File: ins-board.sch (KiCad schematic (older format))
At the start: 83 parts, among them P1 POWER, Q1 FDN306P, Q2 FDC638APZ, Q3 MOSFET_P, U1 24LC128, U2 STM32F415RGT6, U3 LTC4412, U4 MAX3051, U5 LT1965, U6 LT1761-3.3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

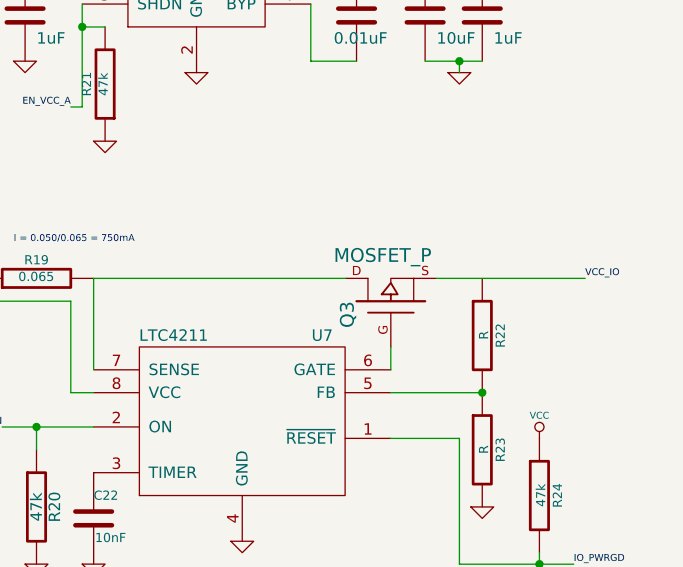
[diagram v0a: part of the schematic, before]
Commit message: add mosfet for current limiter
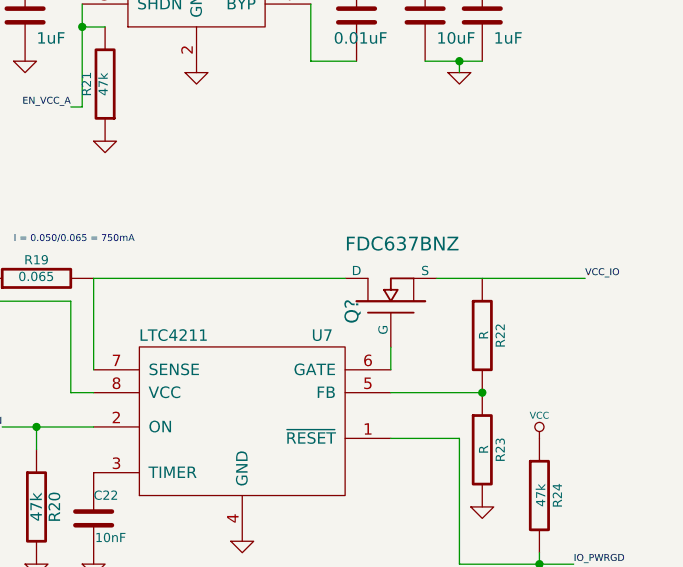
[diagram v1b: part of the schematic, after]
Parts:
- removed Q3: MOSFET_P, ~, symbol MOSFET_P
- added Q?: FDC637BNZ, ~, symbol MOSFET_N
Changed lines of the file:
@@
-$EndComp
-$Comp
-L MOSFET_P Q3
-U 1 1 519731AD
-P 9700 5800
-F 0 "Q3" H 9700 5990 60  0000 R CNN
-F 1 "MOSFET_P" V 9900 6050 60  0000 R CNN
-F 2 "~" H 9700 5800 60  0000 C CNN
-F 3 "~" H 9700 5800 60  0000 C CNN
-	1    9700 5800
-	0    -1   -1   0
 $EndComp
 $Comp
@@
 Text Notes 4450 6300 0    20   ~ 0
 needed for ST USB-Bootloader
+$Comp
+L MOSFET_N Q?
+U 1 1 5197C0F0
+P 9700 5800
+F 0 "Q?" H 9710 5970 60  0000 R CNN
+F 1 "FDC637BNZ" V 9950 6000 60  0000 R CNN
+F 2 "~" H 9700 5800 60  0000 C CNN
+F 3 "~" H 9700 5800 60  0000 C CNN
+	1    9700 5800
+	0    -1   -1   0
+$EndComp
 $EndSCHEMATC

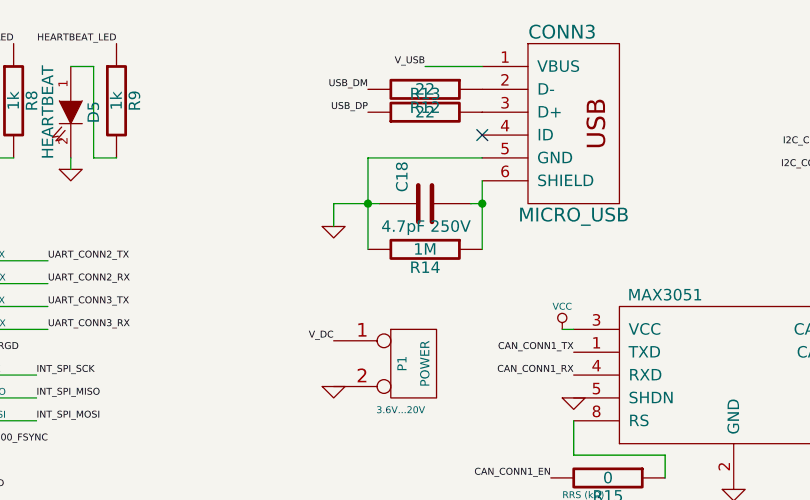
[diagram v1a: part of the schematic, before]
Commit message: remove usb shield connection
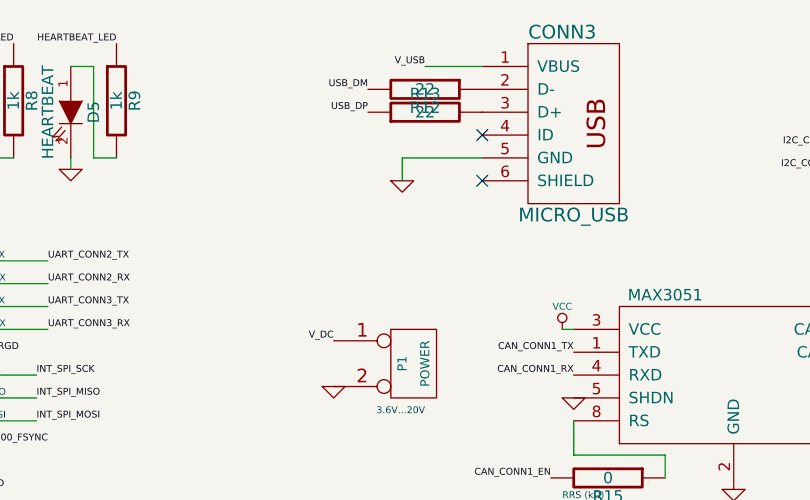
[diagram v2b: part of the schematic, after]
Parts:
- removed C18: 4.7pF 250V, symbol C
- removed R14: 1M, symbol R
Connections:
- wire segments 166 -> 162
- no-connect marks 2 -> 3
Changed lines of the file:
@@
 Sheet 1 2
 Title "INS BOARD"
-Date "18 may 2013"
+Date "17 may 2013"
 Rev "REV A"
 Comp ""
@@
 NoConn ~ 6200 1150
 $Comp
-L MICRO_USB CONN3
-U 1 1 517D9D13
-P 6550 1100
-F 0 "CONN3" H 6550 1500 60  0000 C CNN
-F 1 "MICRO_USB" H 6600 700 60  0000 C CNN
-F 2 "" H 6550 1100 60  0001 C CNN
-F 3 "ZX62-B-5PA(11)" H 6550 1100 60  0001 C CNN
-	1    6550 1100
-	1    0    0    -1
-$EndComp
-$Comp
 L VCC #PWR017
 U 1 1 517D7F9D
@@
 L GND #PWR021
 U 1 1 51295E18
-P 5550 1550
-F 0 "#PWR021" H 5550 1550 30  0001 C CNN
-F 1 "GND" H 5550 1480 30  0001 C CNN
-F 2 "" H 5550 1550 60  0001 C CNN
-F 3 "" H 5550 1550 60  0001 C CNN
-	1    5550 1550
-	1    0    0    -1
-$EndComp
-$Comp
-L C C18
-U 1 1 51295DDF
-P 5950 1450
-F 0 "C18" H 6000 1550 50  0000 L CNN
-F 1 "4.7pF 250V" V 5850 1250 50  0000 L CNN
-F 2 "" H 5950 1450 60  0001 C CNN
-F 3 "" H 5950 1450 60  0001 C CNN
-	1    5950 1450
-	0    -1   -1   0
-$EndComp
-$Comp
-L R R14
-U 1 1 51295DD1
-P 5950 1650
-F 0 "R14" V 6030 1650 50  0000 C CNN
-F 1 "1M" V 5950 1650 50  0000 C CNN
-F 2 "" H 5950 1650 60  0001 C CNN
-F 3 "" H 5950 1650 60  0001 C CNN
-	1    5950 1650
-	0    1    1    0
+P 5850 1350
+F 0 "#PWR021" H 5850 1350 30  0001 C CNN
+F 1 "GND" H 5850 1280 30  0001 C CNN
+F 2 "" H 5850 1350 60  0001 C CNN
+F 3 "" H 5850 1350 60  0001 C CNN
+	1    5850 1350
+	1    0    0    -1
 $EndComp
 $Comp
@@
 	5950 850  6200 850
 Wire Wire Line
-	5550 1550 5550 1450
-Wire Wire Line
-	5550 1450 5750 1450
-Wire Wire Line
-	6200 1250 5700 1250
-Wire Wire Line
-	5700 1250 5700 1650
-Wire Wire Line
-	6200 1350 6200 1650
-Wire Wire Line
 	2450 2400 800  2400
 Wire Wire Line
@@
 	800  2800 2450 2800
 Connection ~ 900  5850
-Wire Wire Line
-	6150 1450 6200 1450
-Connection ~ 6200 1450
-Connection ~ 5700 1450
 Wire Wire Line
 	4950 7300 4800 7300
@@
 	0    -1   -1   0
 $EndComp
+$Comp
+L MICRO_USB CONN3
+U 1 1 517D9D13
+P 6550 1100
+F 0 "CONN3" H 6550 1500 60  0000 C CNN
+F 1 "MICRO_USB" H 6600 700 60  0000 C CNN
+F 2 "" H 6550 1100 60  0001 C CNN
+F 3 "ZX62-B-5PA(11)" H 6550 1100 60  0001 C CNN
+	1    6550 1100
+	1    0    0    -1
+$EndComp
+Wire Wire Line
+	5850 1350 5850 1250
+Wire Wire Line
+	5850 1250 6200 1250
+NoConn ~ 6200 1350
 $EndSCHEMATC

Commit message: fix errors detected by ERC
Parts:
- gave numbers to parts that had none: 2
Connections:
- no-connect marks 3 -> 4
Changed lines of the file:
@@
 Connection ~ 10100 6200
 $Comp
-L R R?
+L R R14
 U 1 1 5197DCCF
 P 4650 6200
-F 0 "R?" V 4730 6200 40  0000 C CNN
+F 0 "R14" V 4730 6200 40  0000 C CNN
 F 1 "47k" V 4657 6201 40  0000 C CNN
 F 2 "~" V 4580 6200 30  0000 C CNN
@@
 	3950 6200 4400 6200
 $Comp
-L VCC #PWR?
+L VCC #PWR057
 U 1 1 5197E9D6
 P 4900 6150
-F 0 "#PWR?" H 4900 6250 30  0001 C CNN
+F 0 "#PWR057" H 4900 6250 30  0001 C CNN
 F 1 "VCC" H 4900 6250 30  0000 C CNN
 F 2 "" H 4900 6150 60  0000 C CNN
@@
 needed for ST USB-Bootloader
 $Comp
-L MOSFET_N Q?
+L MOSFET_N Q3
 U 1 1 5197C0F0
 P 9700 5800
-F 0 "Q?" H 9710 5970 60  0000 R CNN
+F 0 "Q3" H 9710 5970 60  0000 R CNN
 F 1 "FDC637BNZ" V 9950 6000 60  0000 R CNN
 F 2 "~" H 9700 5800 60  0000 C CNN
@@
 	5850 1250 6200 1250
 NoConn ~ 6200 1350
+Connection ~ 10100 5700
+NoConn ~ 3950 5200
+Connection ~ 6750 3250
+Connection ~ 650  4850
 $EndSCHEMATC

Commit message: replaced crystal symbol
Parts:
- removed X1: CRYSTAL 16MHz 20ppm, symbol CRYSTAL
- added X1: CRYSTAL 16MHz 10ppm, symbol XTAL-SMD-4-PADS
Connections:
- wire segments 162 -> 163

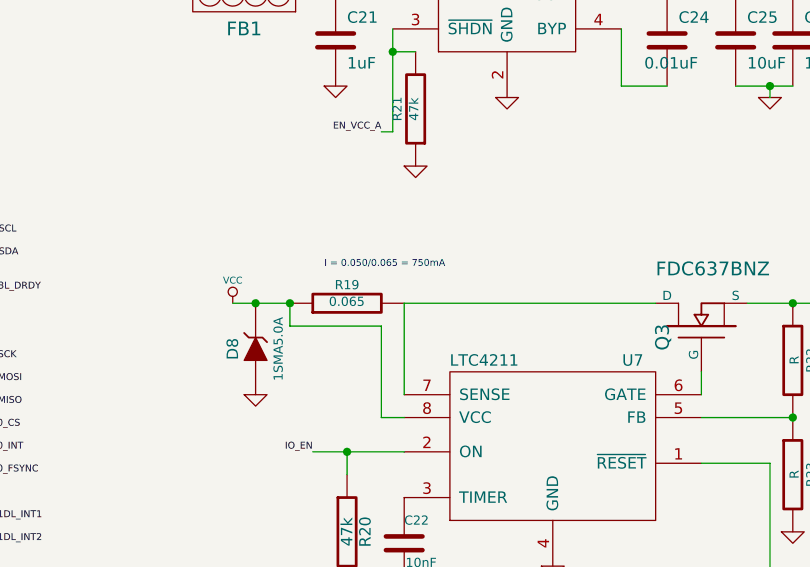
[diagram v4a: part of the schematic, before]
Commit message: changed shunt resistor to 68mOhm, 0603
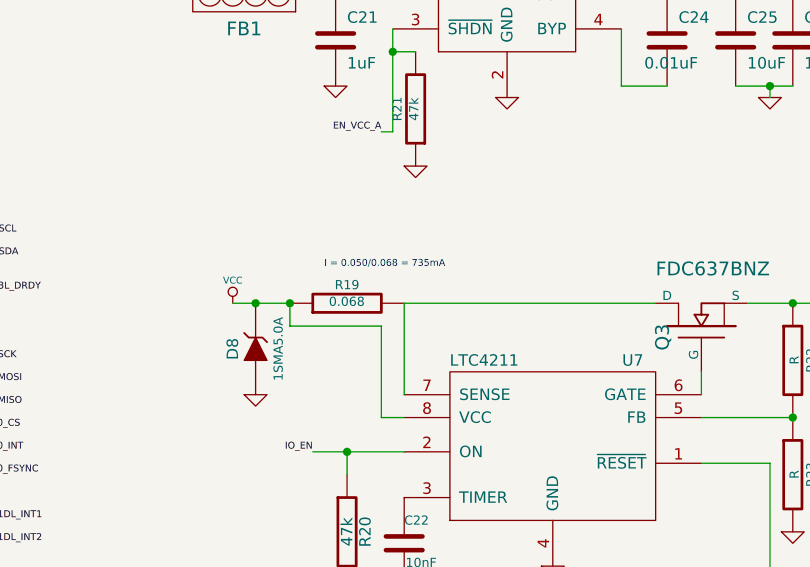
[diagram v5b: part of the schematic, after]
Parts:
- R19: value 0.065 -> 0.068
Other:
- note added: "I = 0.050/0.068 = 735mA"
- note removed: "I = 0.050/0.065 = 750mA"
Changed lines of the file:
@@
 LIBS:linear-regulators
 LIBS:ins-board-cache
-EELAYER 24 0
+EELAYER 27 0
 EELAYER END
 $Descr A4 11693 8268
@@
 P 8150 5700
 F 0 "R19" V 8230 5700 40  0000 C CNN
-F 1 "0.065" V 8157 5701 40  0000 C CNN
+F 1 "0.068" V 8157 5701 40  0000 C CNN
 F 2 "~" V 8080 5700 30  0000 C CNN
 F 3 "~" H 8150 5700 30  0000 C CNN
@@
 $EndComp
 Text Notes 8050 5550 0    30   ~ 0
-I = 0.050/0.065 = 750mA
+I = 0.050/0.068 = 735mA
 $Comp
 L R R20

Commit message: switched to renamed component and footprint libraries
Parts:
- CONN1: symbol JTAG -> _JTAG
- CONN2: symbol MICRO_SD -> _MICRO_SD
- CONN3: symbol MICRO_USB -> _MICRO_USB
- CONN4: symbol I2C -> _I2C
- CONN5: symbol CAN -> _CAN
- CONN6, CONN7, CONN8, CONN9: symbol UART -> _UART
- U1: symbol 24LC128 -> _24LC128
- U2: symbol STM32F415RGT6 -> _STM32F415RGT6
- U3: symbol LTC4412 -> _LTC4412
- U4: symbol MAX3051 -> _MAX3051
- U5: symbol LT1965 -> _LT1965
- U6: symbol LT1761-3.3 -> _LT1761-3.3
- U7: symbol LTC4211 -> _LTC4211
- X1: symbol XTAL-SMD-4-PADS -> _XTAL-SMD-4-PADS
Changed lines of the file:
@@
 LIBS:contrib
 LIBS:valves
-LIBS:connectors
-LIBS:div
-LIBS:sensors
-LIBS:stm32
-LIBS:linear-regulators
+LIBS:_connectors
+LIBS:_div
+LIBS:_sensors
+LIBS:_stm32
+LIBS:_linear-regulators
 LIBS:ins-board-cache
 EELAYER 27 0
@@
 NoConn ~ 6500 4350
 $Comp
-L LTC4412 U3
+L _LTC4412 U3
 U 1 1 518B392C
 P 6000 4250
@@
 V_IN
 $Comp
-L LT1965 U5
+L _LT1965 U5
 U 1 1 518B2FD3
 P 8800 3400
@@
 $EndComp
 $Comp
-L LT1761-3.3 U6
+L _LT1761-3.3 U6
 U 1 1 518B2AA8
 P 8850 4450
@@
 $EndComp
 $Comp
-L 24LC128 U1
+L _24LC128 U1
 U 1 1 518B0384
 P 1400 7150
@@
 $EndComp
 $Comp
-L UART CONN9
+L _UART CONN9
 U 1 1 51292600
 P 10750 2150
@@
 $EndComp
 $Comp
-L UART CONN8
+L _UART CONN8
 U 1 1 512925FD
 P 10750 1150
@@
 $EndComp
 $Comp
-L UART CONN7
+L _UART CONN7
 U 1 1 512925F5
 P 9800 2150
@@
 $EndComp
 $Comp
-L UART CONN6
+L _UART CONN6
 U 1 1 512925F1
 P 9800 1150
@@
 $EndComp
 $Comp
-L JTAG CONN1
+L _JTAG CONN1
 U 1 1 51292368
 P 1300 3700
@@
 $EndComp
 $Comp
-L CAN CONN5
+L _CAN CONN5
 U 1 1 51292362
 P 8700 2150
@@
 $EndComp
 $Comp
-L I2C CONN4
+L _I2C CONN4
 U 1 1 51292359
 P 8700 1150
@@
 $EndComp
 $Comp
-L MAX3051 U4
+L _MAX3051 U4
 U 1 1 518B2D8B
 P 7300 2200
@@
 $EndComp
 $Comp
-L STM32F415RGT6 U2
+L _STM32F415RGT6 U2
 U 1 1 5128F816
 P 3200 4550
@@
 $EndComp
 $Comp
-L MICRO_SD CONN2
+L _MICRO_SD CONN2
 U 1 1 51294CD8
 P 2050 5600
@@
 $EndComp
 $Comp
-L LTC4211 U7
+L _LTC4211 U7
 U 1 1 519731A6
 P 9050 6350
@@
 $EndComp
 $Comp
-L MICRO_USB CONN3
+L _MICRO_USB CONN3
 U 1 1 517D9D13
 P 6550 1100
@@
 Connection ~ 650  4850
 $Comp
-L XTAL-SMD-4-PADS X1
+L _XTAL-SMD-4-PADS X1
 U 1 1 52F50C2D
 P 4250 7300

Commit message: new power design
- separate voltage regulator for io-connectors (powered from DC-in only)
- removed io hot-swap controller
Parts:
- removed C22: 10nF, ~, symbol C
- removed D8: 1SMA5.0A, symbol ZENER
- removed Q3: FDC637BNZ, ~, symbol MOSFET_N
- removed R19: 0.068, ~, symbol R
- removed R22, R23: R, ~, symbol R
- removed R24: 47k, ~, symbol R
- removed U7: LTC4211, MODULE, symbol _LTC4211
- added C? (x2): 10uF, ~, symbol C
- added U?: _LT1965, MODULE, symbol _LT1965
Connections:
- net labels removed: IO_PWRGD
- wire segments 163 -> 154
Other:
- note removed: "(replace with LT3971-3.3)"
- note removed: "I = 0.050/0.068 = 735mA"
- moved on the sheet: C20, C21, C23, C24, C25, C26, C27, FB1, R20, R21

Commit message: updated annotation, added MOSFET footprints
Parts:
- U7: renamed from U?; value _LT1965 -> LT1965
- gave numbers to parts that had none: 2
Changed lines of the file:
@@
 LIBS:_linear-regulators
 LIBS:ins-board-cache
-EELAYER 27 0
+EELAYER 24 0
 EELAYER END
 $Descr A4 11693 8268
@@
 $EndComp
 $Comp
-L GND #PWR51
+L GND #PWR53
 U 1 1 518B3227
 P 10550 3650
-F 0 "#PWR51" H 10550 3650 30  0001 C CNN
+F 0 "#PWR53" H 10550 3650 30  0001 C CNN
 F 1 "GND" H 10550 3580 30  0001 C CNN
 F 2 "" H 10550 3650 60  0001 C CNN
@@
 IO_EN
 $Comp
-L GND #PWR50
+L GND #PWR49
 U 1 1 518B3133
 P 10000 6100
-F 0 "#PWR50" H 10000 6100 30  0001 C CNN
+F 0 "#PWR49" H 10000 6100 30  0001 C CNN
 F 1 "GND" H 10000 6030 30  0001 C CNN
 F 2 "" H 10000 6100 60  0001 C CNN
@@
 $EndComp
 $Comp
-L GND #PWR38
+L GND #PWR36
 U 1 1 518B30D4
 P 8100 6100
-F 0 "#PWR38" H 8100 6100 30  0001 C CNN
+F 0 "#PWR36" H 8100 6100 30  0001 C CNN
 F 1 "GND" H 8100 6030 30  0001 C CNN
 F 2 "" H 8100 6100 60  0001 C CNN
@@
 $EndComp
 $Comp
-L GND #PWR52
+L GND #PWR50
 U 1 1 518B2C27
 P 10350 4800
-F 0 "#PWR52" H 10350 4800 30  0001 C CNN
+F 0 "#PWR50" H 10350 4800 30  0001 C CNN
 F 1 "GND" H 10350 4730 30  0001 C CNN
 F 2 "" H 10350 4800 60  0001 C CNN
@@
 $EndComp
 $Comp
-L GND #PWR39
+L GND #PWR40
 U 1 1 512960AA
 P 8450 4750
-F 0 "#PWR39" H 8450 4750 30  0001 C CNN
+F 0 "#PWR40" H 8450 4750 30  0001 C CNN
 F 1 "GND" H 8450 4680 30  0001 C CNN
 F 2 "" H 8450 4750 60  0001 C CNN
@@
 $EndComp
 $Comp
-L GND #PWR57
+L GND #PWR52
 U 1 1 51292680
 P 10400 2100
-F 0 "#PWR57" H 10400 2100 30  0001 C CNN
+F 0 "#PWR52" H 10400 2100 30  0001 C CNN
 F 1 "GND" H 10400 2030 30  0001 C CNN
 F 2 "" H 10400 2100 60  0001 C CNN
@@
 $EndComp
 $Comp
-L GND #PWR56
+L GND #PWR51
 U 1 1 51292679
 P 10400 1100
-F 0 "#PWR56" H 10400 1100 30  0001 C CNN
+F 0 "#PWR51" H 10400 1100 30  0001 C CNN
 F 1 "GND" H 10400 1030 30  0001 C CNN
 F 2 "" H 10400 1100 60  0001 C CNN
@@
 $EndComp
 $Comp
-L GND #PWR49
+L GND #PWR47
 U 1 1 51292677
 P 9450 2100
-F 0 "#PWR49" H 9450 2100 30  0001 C CNN
+F 0 "#PWR47" H 9450 2100 30  0001 C CNN
 F 1 "GND" H 9450 2030 30  0001 C CNN
 F 2 "" H 9450 2100 60  0001 C CNN
@@
 $EndComp
 $Comp
-L GND #PWR48
+L GND #PWR46
 U 1 1 51292672
 P 9450 1100
-F 0 "#PWR48" H 9450 1100 30  0001 C CNN
+F 0 "#PWR46" H 9450 1100 30  0001 C CNN
 F 1 "GND" H 9450 1030 30  0001 C CNN
 F 2 "" H 9450 1100 60  0001 C CNN
@@
 $EndComp
 $Comp
-L GND #PWR42
+L GND #PWR39
 U 1 1 5129266F
 P 8350 2100
-F 0 "#PWR42" H 8350 2100 30  0001 C CNN
+F 0 "#PWR39" H 8350 2100 30  0001 C CNN
 F 1 "GND" H 8350 2030 30  0001 C CNN
 F 2 "" H 8350 2100 60  0001 C CNN
@@
 $EndComp
 $Comp
-L GND #PWR41
+L GND #PWR38
 U 1 1 51292667
 P 8350 1100
-F 0 "#PWR41" H 8350 1100 30  0001 C CNN
+F 0 "#PWR38" H 8350 1100 30  0001 C CNN
 F 1 "GND" H 8350 1030 30  0001 C CNN
 F 2 "" H 8350 1100 60  0001 C CNN
@@
 $EndComp
 $Comp
-L GND #PWR44
+L GND #PWR42
 U 1 1 519876CA
 P 8800 5100
-F 0 "#PWR44" H 8800 5100 30  0001 C CNN
+F 0 "#PWR42" H 8800 5100 30  0001 C CNN
 F 1 "GND" H 8800 5030 30  0001 C CNN
 F 2 "" H 8800 5100 60  0000 C CNN
@@
 $EndComp
 $Comp
-L GND #PWR46
+L GND #PWR44
 U 1 1 51987A30
 P 9200 4800
-F 0 "#PWR46" H 9200 4800 30  0001 C CNN
+F 0 "#PWR44" H 9200 4800 30  0001 C CNN
 F 1 "GND" H 9200 4730 30  0001 C CNN
 F 2 "" H 9200 4800 60  0000 C CNN
@@
 Connection ~ 4450 7300
 $Comp
-L GND #PWR40
+L GND #PWR41
 U 1 1 519748B3
 P 8600 6400
-F 0 "#PWR40" H 8600 6400 30  0001 C CNN
+F 0 "#PWR41" H 8600 6400 30  0001 C CNN
 F 1 "GND" H 8600 6330 30  0001 C CNN
 F 2 "" H 8600 6400 60  0000 C CNN
@@
 Connection ~ 8600 5900
 $Comp
-L C C?
+L C C22
 U 1 1 52F727B7
 P 10000 3450
-F 0 "C?" H 10000 3550 40  0000 L CNN
+F 0 "C22" H 10000 3550 40  0000 L CNN
 F 1 "10uF" H 10006 3365 40  0000 L CNN
 F 2 "~" H 10038 3300 30  0000 C CNN
@@
 Connection ~ 10000 3250
 $Comp
-L GND #PWR?
+L GND #PWR48
 U 1 1 52F72B6D
 P 10000 3650
-F 0 "#PWR?" H 10000 3650 30  0001 C CNN
+F 0 "#PWR48" H 10000 3650 30  0001 C CNN
 F 1 "GND" H 10000 3580 30  0001 C CNN
 F 2 "" H 10000 3650 60  0000 C CNN
@@
 $EndComp
 $Comp
-L C C?
+L C C18
 U 1 1 52F72BCA
 P 8300 3450
-F 0 "C?" H 8300 3550 40  0000 L CNN
+F 0 "C18" H 8300 3550 40  0000 L CNN
 F 1 "10uF" H 8306 3365 40  0000 L CNN
 F 2 "~" H 8338 3300 30  0000 C CNN
@@
 $EndComp
 $Comp
-L GND #PWR?
+L GND #PWR37
 U 1 1 52F72C05
 P 8300 3650
-F 0 "#PWR?" H 8300 3650 30  0001 C CNN
+F 0 "#PWR37" H 8300 3650 30  0001 C CNN
 F 1 "GND" H 8300 3580 30  0001 C CNN
 F 2 "" H 8300 3650 60  0000 C CNN
@@
 Connection ~ 8300 3250
 $Comp
-L _LT1965 U?
+L _LT1965 U7
 U 1 1 52F73BF5
 P 9150 3400
-F 0 "U?" H 9500 3700 50  0000 C CNN
-F 1 "_LT1965" H 8900 3700 50  0000 C CNN
+F 0 "U7" H 9500 3700 50  0000 C CNN
+F 1 "LT1965" H 8900 3700 50  0000 C CNN
 F 2 "MODULE" H 9150 3500 50  0001 C CNN
 F 3 "DOCUMENTATION" H 9150 3500 50  0001 C CNN
@@
 $EndComp
 $Comp
-L GND #PWR?
+L GND #PWR43
 U 1 1 52F7403F
 P 9150 3950
-F 0 "#PWR?" H 9150 3950 30  0001 C CNN
+F 0 "#PWR43" H 9150 3950 30  0001 C CNN
 F 1 "GND" H 9150 3880 30  0001 C CNN
 F 2 "" H 9150 3950 60  0000 C CNN
